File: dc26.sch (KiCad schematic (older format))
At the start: 60 parts, among them J1 CONN_01X10, J2 CONN_01X10, J3 CONN_01X10, Y1 Crystal

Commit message: Further updates
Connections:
- net +5V: now also B_SHIFT_1.16 (VCC), B_SHIFT_2.16 (VCC)
- net GND: now also B_SHIFT_1.8 (GND), B_SHIFT_2.8 (GND)
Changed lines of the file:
@@
 $EndDescr
-$Comp
-L 74LS165 B_SHIFT_1
-U 1 1 5ACD7519
-P -1800 -5700
-F 0 "B_SHIFT_1" H -1650 -5750 50  0000 C CNN
-F 1 "74LS165" H -1650 -5950 50  0000 C CNN
-F 2 "Housings_SSOP:TSSOP-16_4.4x5mm_Pitch0.65mm" H -1800 -5700 50  0001 C CNN
-F 3 "" H -1800 -5700 50  0001 C CNN
-	1    -1800 -5700
-	1    0    0    -1
-$EndComp
 $Comp
 L 74LS165 B_SHIFT_2
@@
 $EndComp
 $Comp
-L GND #PWR18
+L GND #PWR01
 U 1 1 5AD27FBE
-P -3800 -6700
-F 0 "#PWR18" H -3800 -6950 50  0001 C CNN
-F 1 "GND" H -3800 -6850 50  0000 C CNN
-F 2 "" H -3800 -6700 50  0001 C CNN
-F 3 "" H -3800 -6700 50  0001 C CNN
-	1    -3800 -6700
-	-1   0    0    1
-$EndComp
-$Comp
-L GND #PWR2
+P -3450 -6450
+F 0 "#PWR01" H -3450 -6700 50  0001 C CNN
+F 1 "GND" H -3450 -6600 50  0000 C CNN
+F 2 "" H -3450 -6450 50  0001 C CNN
+F 3 "" H -3450 -6450 50  0001 C CNN
+	1    -3450 -6450
+	1    0    0    -1
+$EndComp
+$Comp
+L GND #PWR02
 U 1 1 5AD5BD83
 P -12550 1050
-F 0 "#PWR2" H -12550 800 50  0001 C CNN
+F 0 "#PWR02" H -12550 800 50  0001 C CNN
 F 1 "GND" H -12550 900 50  0000 C CNN
 F 2 "" H -12550 1050 50  0001 C CNN
@@
 $EndComp
 $Comp
-L VCC #PWR6
+L VCC #PWR03
 U 1 1 5AD5C4E4
 P -12300 1050
-F 0 "#PWR6" H -12300 900 50  0001 C CNN
+F 0 "#PWR03" H -12300 900 50  0001 C CNN
 F 1 "VCC" H -12300 1200 50  0000 C CNN
 F 2 "" H -12300 1050 50  0001 C CNN
@@
 $EndComp
 $Comp
-L GND #PWR20
+L GND #PWR04
 U 1 1 5AD6E593
 P -2500 -5100
-F 0 "#PWR20" H -2500 -5350 50  0001 C CNN
+F 0 "#PWR04" H -2500 -5350 50  0001 C CNN
 F 1 "GND" H -2500 -5250 50  0000 C CNN
 F 2 "" H -2500 -5100 50  0001 C CNN
@@
 $EndComp
 $Comp
-L GND #PWR21
+L GND #PWR05
 U 1 1 5AD6F999
 P -2500 -3550
-F 0 "#PWR21" H -2500 -3800 50  0001 C CNN
+F 0 "#PWR05" H -2500 -3800 50  0001 C CNN
 F 1 "GND" H -2500 -3700 50  0000 C CNN
 F 2 "" H -2500 -3550 50  0001 C CNN
@@
 $EndComp
 $Comp
-L GND #PWR19
+L GND #PWR06
 U 1 1 5AD77A72
 P -3600 -800
-F 0 "#PWR19" H -3600 -1050 50  0001 C CNN
+F 0 "#PWR06" H -3600 -1050 50  0001 C CNN
 F 1 "GND" H -3600 -950 50  0000 C CNN
 F 2 "" H -3600 -800 50  0001 C CNN
@@
 $EndComp
 $Comp
-L VCC #PWR11
+L VCC #PWR07
 U 1 1 5AD946E2
 P -7100 12550
-F 0 "#PWR11" H -7100 12400 50  0001 C CNN
+F 0 "#PWR07" H -7100 12400 50  0001 C CNN
 F 1 "VCC" H -7100 12700 50  0000 C CNN
 F 2 "" H -7100 12550 50  0001 C CNN
@@
 $EndComp
 $Comp
-L GND #PWR10
+L GND #PWR08
 U 1 1 5AD98D43
 P -7100 12200
-F 0 "#PWR10" H -7100 11950 50  0001 C CNN
+F 0 "#PWR08" H -7100 11950 50  0001 C CNN
 F 1 "GND" H -7100 12050 50  0000 C CNN
 F 2 "" H -7100 12200 50  0001 C CNN
@@
 $EndComp
 $Comp
-L GND #PWR17
+L GND #PWR09
 U 1 1 5ADAF5CF
 P -3950 10600
-F 0 "#PWR17" H -3950 10350 50  0001 C CNN
+F 0 "#PWR09" H -3950 10350 50  0001 C CNN
 F 1 "GND" H -3950 10450 50  0000 C CNN
 F 2 "" H -3950 10600 50  0001 C CNN
@@
 $EndComp
 $Comp
-L GND #PWR15
+L GND #PWR010
 U 1 1 5ADAFD4C
 P -4000 9500
-F 0 "#PWR15" H -4000 9250 50  0001 C CNN
+F 0 "#PWR010" H -4000 9250 50  0001 C CNN
 F 1 "GND" H -4000 9350 50  0000 C CNN
 F 2 "" H -4000 9500 50  0001 C CNN
@@
 $EndComp
 $Comp
-L GND #PWR16
+L GND #PWR011
 U 1 1 5ADB04C2
 P -4000 12400
-F 0 "#PWR16" H -4000 12150 50  0001 C CNN
+F 0 "#PWR011" H -4000 12150 50  0001 C CNN
 F 1 "GND" H -4000 12250 50  0000 C CNN
 F 2 "" H -4000 12400 50  0001 C CNN
@@
 $EndComp
 $Comp
-L GND #PWR12
+L GND #PWR012
 U 1 1 5B04F2A2
 P -7000 8800
-F 0 "#PWR12" H -7000 8550 50  0001 C CNN
+F 0 "#PWR012" H -7000 8550 50  0001 C CNN
 F 1 "GND" H -7000 8650 50  0000 C CNN
 F 2 "" H -7000 8800 50  0001 C CNN
@@
 $EndComp
 $Comp
-L GND #PWR1
+L GND #PWR013
 U 1 1 5B0E23AB
 P -13400 6550
-F 0 "#PWR1" H -13400 6300 50  0001 C CNN
+F 0 "#PWR013" H -13400 6300 50  0001 C CNN
 F 1 "GND" H -13400 6400 50  0000 C CNN
 F 2 "" H -13400 6550 50  0001 C CNN
@@
 $EndComp
 $Comp
-L +3.3V #PWR9
+L +3.3V #PWR014
 U 1 1 5B0D3E01
 P -7200 2050
-F 0 "#PWR9" H -7200 1900 50  0001 C CNN
+F 0 "#PWR014" H -7200 1900 50  0001 C CNN
 F 1 "+3.3V" H -7200 2190 50  0000 C CNN
 F 2 "" H -7200 2050 50  0001 C CNN
@@
 $EndComp
 $Comp
-L GND #PWR7
+L GND #PWR015
 U 1 1 5B0F137D
 P -12250 5250
-F 0 "#PWR7" H -12250 5000 50  0001 C CNN
+F 0 "#PWR015" H -12250 5000 50  0001 C CNN
 F 1 "GND" H -12250 5100 50  0000 C CNN
 F 2 "" H -12250 5250 50  0001 C CNN
@@
 $EndComp
 $Comp
-L GND #PWR13
+L GND #PWR016
 U 1 1 5B0F6A9C
 P -6200 3750
-F 0 "#PWR13" H -6200 3500 50  0001 C CNN
+F 0 "#PWR016" H -6200 3500 50  0001 C CNN
 F 1 "GND" H -6200 3600 50  0000 C CNN
 F 2 "" H -6200 3750 50  0001 C CNN
@@
 $EndComp
 $Comp
-L +3.3V #PWR8
+L +3.3V #PWR017
 U 1 1 5B11C638
 P -11750 3950
-F 0 "#PWR8" H -11750 3800 50  0001 C CNN
+F 0 "#PWR017" H -11750 3800 50  0001 C CNN
 F 1 "+3.3V" H -11750 4090 50  0000 C CNN
 F 2 "" H -11750 3950 50  0001 C CNN
@@
 $EndComp
 $Comp
-L GND #PWR5
+L GND #PWR018
 U 1 1 5B12677B
 P -12400 4350
-F 0 "#PWR5" H -12400 4100 50  0001 C CNN
+F 0 "#PWR018" H -12400 4100 50  0001 C CNN
 F 1 "GND" H -12400 4200 50  0000 C CNN
 F 2 "" H -12400 4350 50  0001 C CNN
@@
 $EndComp
 $Comp
-L GND #PWR4
+L GND #PWR019
 U 1 1 5B1309D3
 P -12450 4950
-F 0 "#PWR4" H -12450 4700 50  0001 C CNN
+F 0 "#PWR019" H -12450 4700 50  0001 C CNN
 F 1 "GND" H -12450 4800 50  0000 C CNN
 F 2 "" H -12450 4950 50  0001 C CNN
@@
 $EndComp
 $Comp
-L +3.3V #PWR3
+L +3.3V #PWR020
 U 1 1 5B136E3C
 P -12450 4750
-F 0 "#PWR3" H -12450 4600 50  0001 C CNN
+F 0 "#PWR020" H -12450 4600 50  0001 C CNN
 F 1 "+3.3V" H -12450 4890 50  0000 C CNN
 F 2 "" H -12450 4750 50  0001 C CNN
@@
 $EndComp
 $Comp
-L GND #PWR22
+L GND #PWR021
 U 1 1 5B13B631
 P -1800 6650
-F 0 "#PWR22" H -1800 6400 50  0001 C CNN
+F 0 "#PWR021" H -1800 6400 50  0001 C CNN
 F 1 "GND" H -1800 6500 50  0000 C CNN
 F 2 "" H -1800 6650 50  0001 C CNN
@@
 $EndComp
 $Comp
-L GND #PWR23
+L GND #PWR022
 U 1 1 5B1B7467
 P -1200 9050
-F 0 "#PWR23" H -1200 8800 50  0001 C CNN
+F 0 "#PWR022" H -1200 8800 50  0001 C CNN
 F 1 "GND" H -1200 8900 50  0000 C CNN
 F 2 "" H -1200 9050 50  0001 C CNN
@@
 Connection ~ -4300 -3750
 Wire Wire Line
-	-3800 -6700 -3800 -6550
-Wire Wire Line
-	-4000 -6550 -3450 -6550
-Wire Wire Line
 	-4000 -6550 -4000 -3900
 Connection ~ -4000 -6250
@@
 Connection ~ -13250 6150
 $Comp
-L +5V #PWR14
+L +5V #PWR023
 U 1 1 5B123F56
 P -5650 -6600
-F 0 "#PWR14" H -5650 -6750 50  0001 C CNN
+F 0 "#PWR023" H -5650 -6750 50  0001 C CNN
 F 1 "+5V" H -5650 -6460 50  0000 C CNN
 F 2 "" H -5650 -6600 50  0001 C CNN
@@
 Wire Wire Line
 	-2700 6250 -1550 6250
-$Comp
-L PWR_FLAG #FLG?
-U 1 1 5B18689B
-P -6050 -6500
-F 0 "#FLG?" H -6050 -6425 50  0001 C CNN
-F 1 "PWR_FLAG" H -6050 -6350 50  0000 C CNN
-F 2 "" H -6050 -6500 50  0001 C CNN
-F 3 "" H -6050 -6500 50  0001 C CNN
-	1    -6050 -6500
-	1    0    0    -1
-$EndComp
-Wire Wire Line
-	-6050 -6450 -5650 -6450
-Connection ~ -5650 -6450
-Wire Wire Line
-	-6050 -6450 -6050 -6500
-$Comp
-L PWR_FLAG #FLG?
-U 1 1 5B18707E
-P -3450 -6550
-F 0 "#FLG?" H -3450 -6475 50  0001 C CNN
-F 1 "PWR_FLAG" H -3450 -6400 50  0000 C CNN
-F 2 "" H -3450 -6550 50  0001 C CNN
-F 3 "" H -3450 -6550 50  0001 C CNN
-	1    -3450 -6550
-	1    0    0    -1
-$EndComp
-Connection ~ -3800 -6550
+Wire Wire Line
+	-4000 -6550 -3450 -6550
+Wire Wire Line
+	-3450 -6550 -3450 -6450
+$Comp
+L GND #PWR?
+U 1 1 5B188D2F
+P -1100 -5650
+F 0 "#PWR?" H -1100 -5900 50  0001 C CNN
+F 1 "GND" H -1100 -5800 50  0000 C CNN
+F 2 "" H -1100 -5650 50  0001 C CNN
+F 3 "" H -1100 -5650 50  0001 C CNN
+	1    -1100 -5650
+	1    0    0    -1
+$EndComp
+$Comp
+L 74LS165 B_SHIFT_1
+U 1 1 5ACD7519
+P -1800 -5700
+F 0 "B_SHIFT_1" H -1650 -5750 50  0000 C CNN
+F 1 "74LS165" H -1650 -5950 50  0000 C CNN
+F 2 "Housings_SSOP:TSSOP-16_4.4x5mm_Pitch0.65mm" H -1800 -5700 50  0001 C CNN
+F 3 "" H -1800 -5700 50  0001 C CNN
+	1    -1800 -5700
+	1    0    0    -1
+$EndComp
+Wire Wire Line
+	-1300 -5700 -1100 -5700
+Wire Wire Line
+	-1100 -5700 -1100 -5650
+$Comp
+L +5V #PWR?
+U 1 1 5B1896AE
+P -1100 -5850
+F 0 "#PWR?" H -1100 -6000 50  0001 C CNN
+F 1 "+5V" H -1100 -5710 50  0000 C CNN
+F 2 "" H -1100 -5850 50  0001 C CNN
+F 3 "" H -1100 -5850 50  0001 C CNN
+	1    -1100 -5850
+	1    0    0    -1
+$EndComp
+Wire Wire Line
+	-1300 -5850 -1100 -5850
+$Comp
+L +5V #PWR?
+U 1 1 5B189C3C
+P -1150 -4300
+F 0 "#PWR?" H -1150 -4450 50  0001 C CNN
+F 1 "+5V" H -1150 -4160 50  0000 C CNN
+F 2 "" H -1150 -4300 50  0001 C CNN
+F 3 "" H -1150 -4300 50  0001 C CNN
+	1    -1150 -4300
+	1    0    0    -1
+$EndComp
+$Comp
+L GND #PWR?
+U 1 1 5B189D37
+P -1150 -4150
+F 0 "#PWR?" H -1150 -4400 50  0001 C CNN
+F 1 "GND" H -1150 -4300 50  0000 C CNN
+F 2 "" H -1150 -4150 50  0001 C CNN
+F 3 "" H -1150 -4150 50  0001 C CNN
+	1    -1150 -4150
+	1    0    0    -1
+$EndComp
+Wire Wire Line
+	-1300 -4300 -1150 -4300
+Wire Wire Line
+	-1150 -4150 -1300 -4150
 $EndSCHEMATC

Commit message: Changing tp silkscreen names
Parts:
- removed CON_IR1: CONN_01X07, Connectors_JST:JST_PH_B8B-PH-SM4-TB_08x2.00mm_Straight, symbol CONN_01X07
- removed IR_RX_F1, IR_RX_L2, IR_RX_R2: TSOP38238, custom-footprints:IR_Receiver, symbol TSOP38238
- removed IR_RX_L1, IR_RX_R1, IR_TX_F1: IR204A, LEDs:LED_0603, symbol IR204A
- removed R1, R2, R3: 100R, Resistors_SMD:R_0603, symbol R
- TP-BOOT0: value TP-BOOT0 -> BOOT0
- TP-BTN-CLK1: value TP-BTN-CLK -> BTN-CLK
- TP-BTN-DATA1: value TP-BTN-DATA -> BTN-DATA
- TP-BTN-GND1: value TP-BTN-GND -> BTN-GND
- TP-BTN-LOAD1: value TP-BTN-LOAD -> BTN-LD
- TP-NRST1: value TP-NRST -> NRST
- TP-PGM-GND1: value TP-PGM-GND -> PGM-GND
- TP-PGM-SWDCLK1: value TP-PGM-SWDCLK -> PGM-SWDCLK
- TP-PGM-SWDIO1: value TP-PGM-SWDIO -> PGM-SWDIO
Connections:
- net IR-TX-R: now reaches J3.5 (P5), STM32F405.29 (I2C2_SCL/I2S2_CK/SPI2_SCK/TIM2_CH3/USART3_TX/USB_OTG_HS_ULPI_D3/PB10)
- net IR-RX-R: now reaches J3.6 (P6), STM32F405.30 (ADC1_EXTI11/ADC2_EXTI11/ADC3_EXTI11/I2C2_SDA/TIM2_CH4/USART3_RX/USB_OTG_HS_ULPI_D4/PB11)
- net IR-TX-F: now reaches J2.10 (P10), STM32F405.51 (PC10/I2S3_CK/SDIO_D2/SPI3_SCK/UART4_TX/USART3_TX)
- net IR-RX-F: now reaches J2.9 (P9), STM32F405.52 (PC11/ADC1_EXTI11/ADC2_EXTI11/ADC3_EXTI11/I2S3_ext_SD/SDIO_D3/SPI3_MISO/UART4_RX/USART3_RX)
- net IR-TX-L: now reaches J3.1 (P1), STM32F405.58 (CAN2_TX/I2C1_SCL/TIM4_CH1/USART1_TX/PB6)
- net IR-RX-L: now reaches J3.2 (P2), STM32F405.59 (I2C1_SDA/TIM4_CH2/USART1_RX/PB7)
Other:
- moved on the sheet: J1, J2

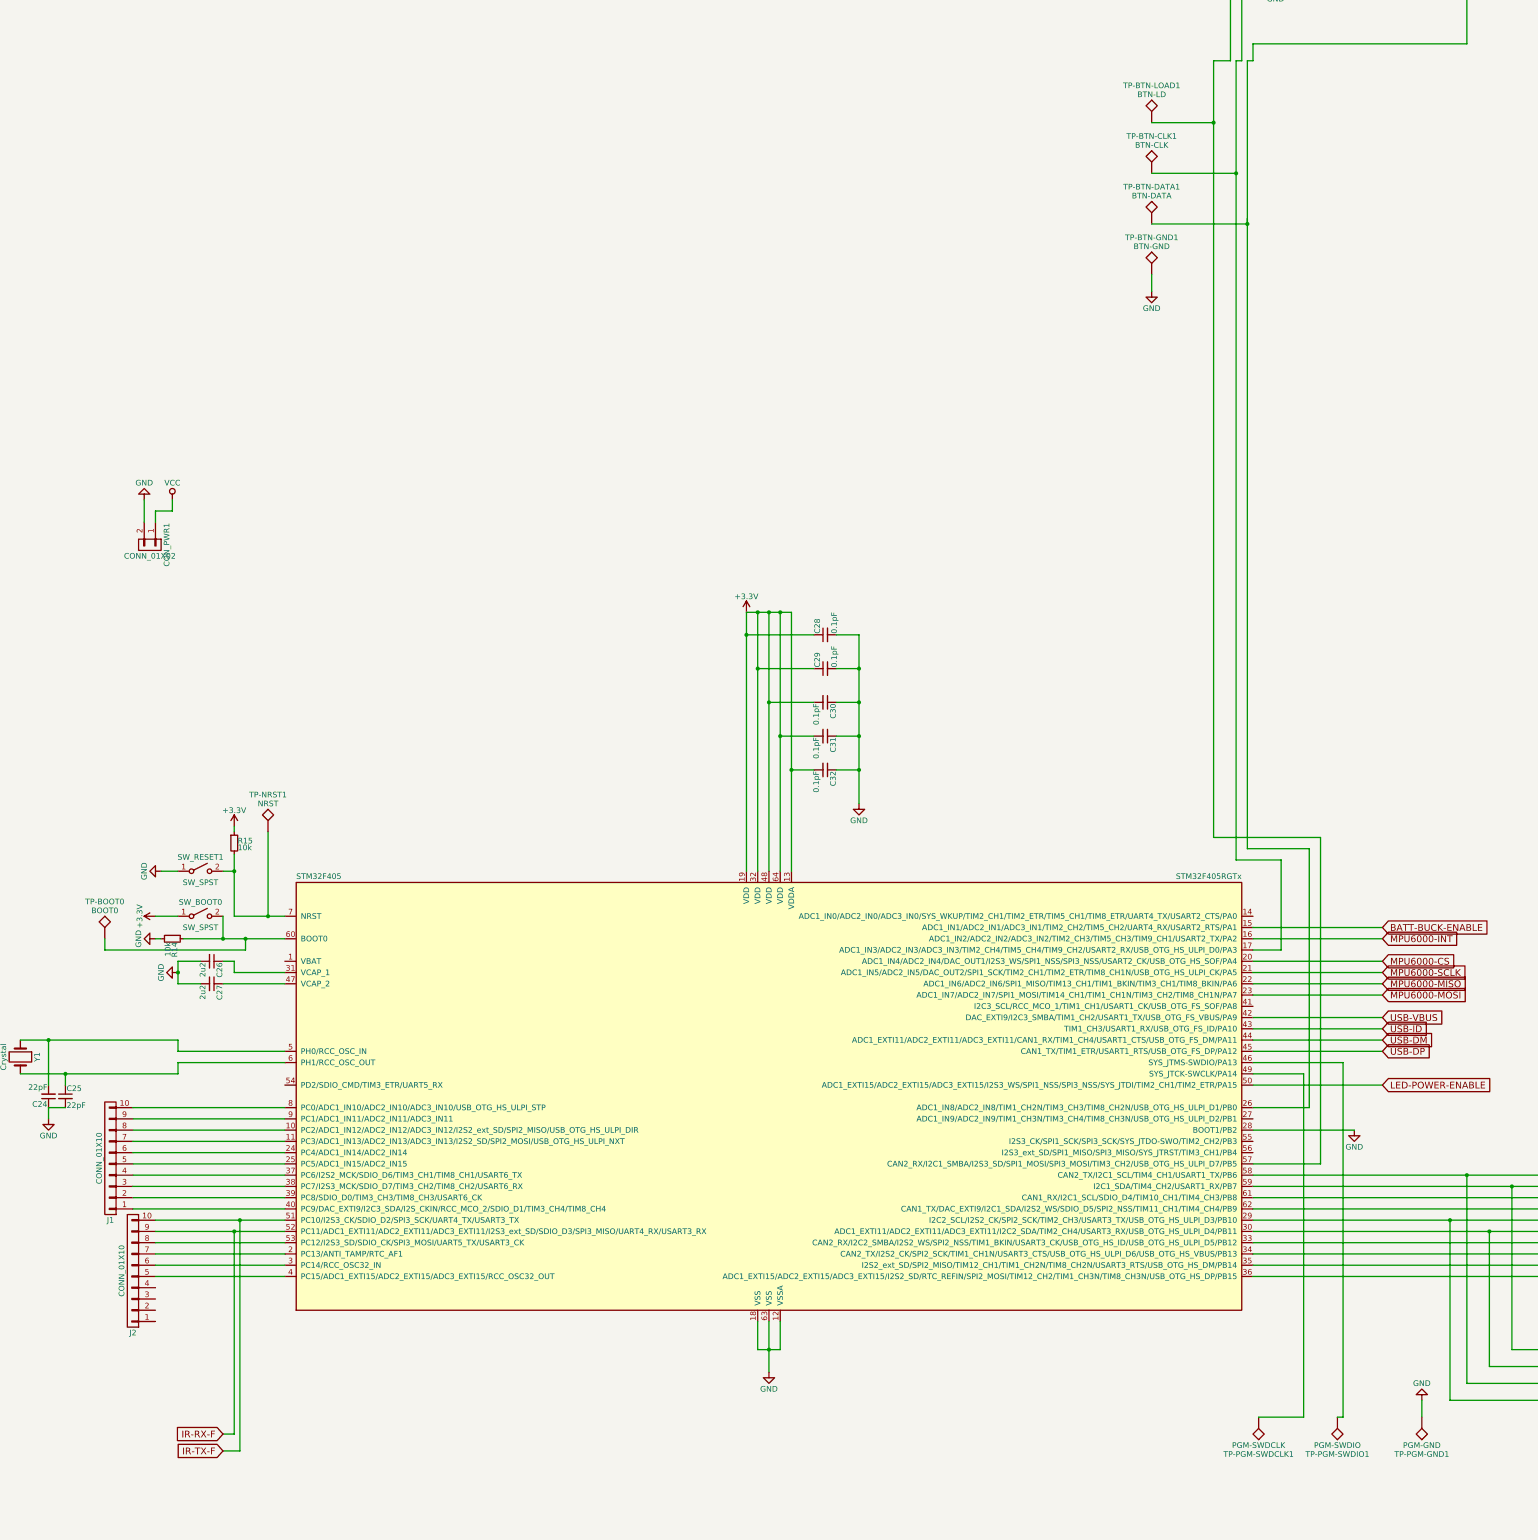
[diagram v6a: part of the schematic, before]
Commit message: tp name fixes
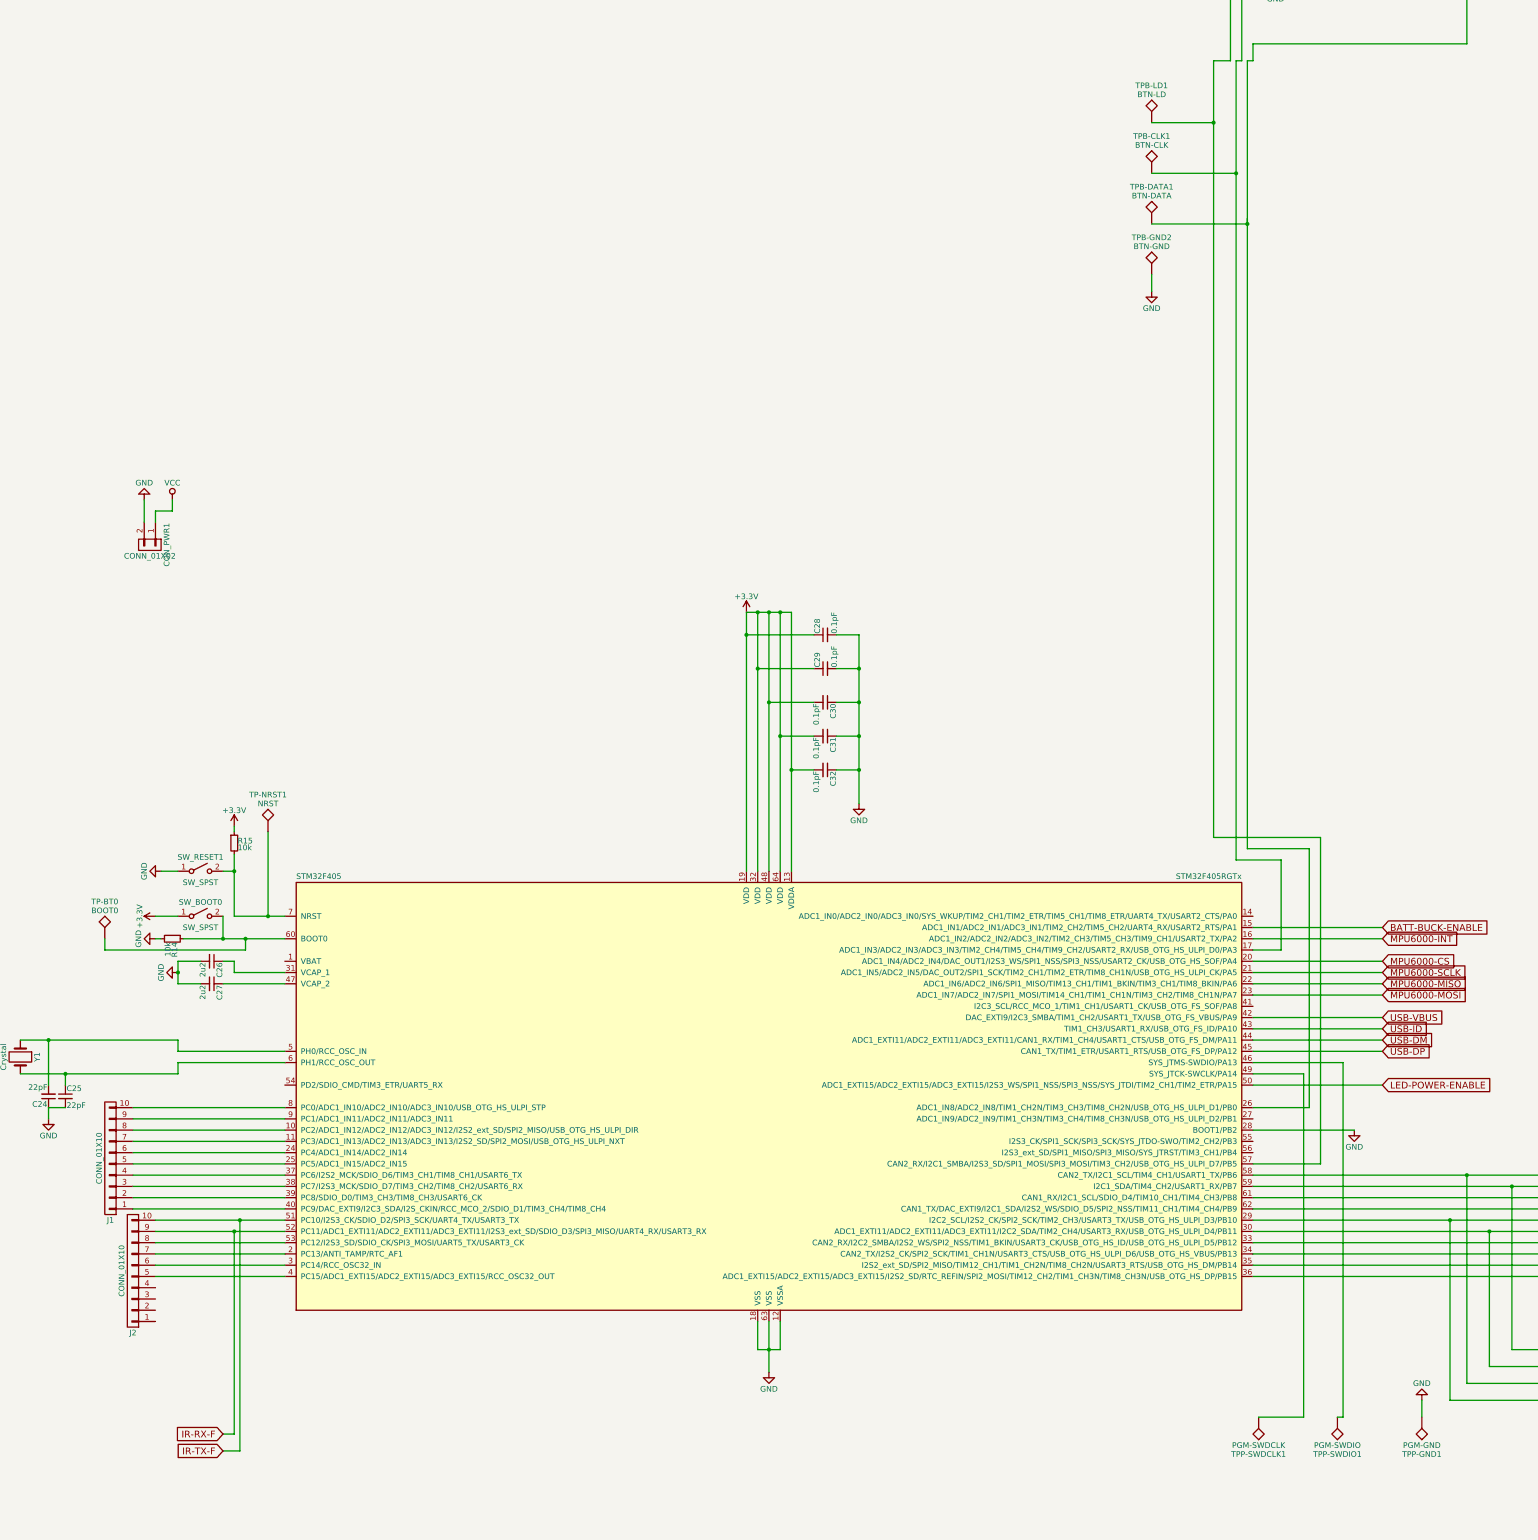
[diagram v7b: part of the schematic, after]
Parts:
- renumbered TP-BOOT0 to TP-BT0, TP-BTN-CLK1 to TPB-CLK1, TP-BTN-DATA1 to TPB-DATA1, TP-BTN-GND1 to TPB-GND2, TP-BTN-LOAD1 to TPB-LD1, TP-PGM-GND1 to TPP-GND1, TP-PGM-SWDCLK1 to TPP-SWDCLK1, TP-PGM-SWDIO1 to TPP-SWDIO1
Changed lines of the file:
@@
 $EndComp
 $Comp
-L TEST TP-PGM-SWDCLK1
+L TEST TPP-SWDCLK1
 U 1 1 5B1B5199
 P -2650 9200
-F 0 "TP-PGM-SWDCLK1" H -2650 9500 50  0000 C BNN
+F 0 "TPP-SWDCLK1" H -2650 9500 50  0000 C BNN
 F 1 "PGM-SWDCLK" H -2650 9450 50  0000 C CNN
 F 2 "Measurement_Points:Measurement_Point_Round-SMD-Pad_Small" H -2650 9200 50  0001 C CNN
@@
 $EndComp
 $Comp
-L TEST TP-PGM-SWDIO1
+L TEST TPP-SWDIO1
 U 1 1 5B1B59E8
 P -1950 9200
-F 0 "TP-PGM-SWDIO1" H -1950 9500 50  0000 C BNN
+F 0 "TPP-SWDIO1" H -1950 9500 50  0000 C BNN
 F 1 "PGM-SWDIO" H -1950 9450 50  0000 C CNN
 F 2 "Measurement_Points:Measurement_Point_Round-SMD-Pad_Small" H -1950 9200 50  0001 C CNN
@@
 $EndComp
 $Comp
-L TEST TP-PGM-GND1
+L TEST TPP-GND1
 U 1 1 5B1B6C72
 P -1200 9200
-F 0 "TP-PGM-GND1" H -1200 9500 50  0000 C BNN
+F 0 "TPP-GND1" H -1200 9500 50  0000 C BNN
 F 1 "PGM-GND" H -1200 9450 50  0000 C CNN
 F 2 "Measurement_Points:Measurement_Point_Round-SMD-Pad_Small" H -1200 9200 50  0001 C CNN
@@
 $EndComp
 $Comp
-L TEST TP-BOOT0
+L TEST TP-BT0
 U 1 1 5B1D1428
 P -12900 4950
-F 0 "TP-BOOT0" H -12900 5250 50  0000 C BNN
+F 0 "TP-BT0" H -12900 5250 50  0000 C BNN
 F 1 "BOOT0" H -12900 5200 50  0000 C CNN
 F 2 "Measurement_Points:Measurement_Point_Round-SMD-Pad_Small" H -12900 4950 50  0001 C CNN
@@
 $EndSheet
 $Comp
-L TEST TP-BTN-LOAD1
+L TEST TPB-LD1
 U 1 1 5B100C70
 P -3600 -2300
-F 0 "TP-BTN-LOAD1" H -3600 -2000 50  0000 C BNN
+F 0 "TPB-LD1" H -3600 -2000 50  0000 C BNN
 F 1 "BTN-LD" H -3600 -2050 50  0000 C CNN
 F 2 "Measurement_Points:Measurement_Point_Round-SMD-Pad_Small" H -3600 -2300 50  0001 C CNN
@@
 $EndComp
 $Comp
-L TEST TP-BTN-CLK1
+L TEST TPB-CLK1
 U 1 1 5B101294
 P -3600 -1850
-F 0 "TP-BTN-CLK1" H -3600 -1550 50  0000 C BNN
+F 0 "TPB-CLK1" H -3600 -1550 50  0000 C BNN
 F 1 "BTN-CLK" H -3600 -1600 50  0000 C CNN
 F 2 "Measurement_Points:Measurement_Point_Round-SMD-Pad_Small" H -3600 -1850 50  0001 C CNN
@@
 $EndComp
 $Comp
-L TEST TP-BTN-DATA1
+L TEST TPB-DATA1
 U 1 1 5B101492
 P -3600 -1400
-F 0 "TP-BTN-DATA1" H -3600 -1100 50  0000 C BNN
+F 0 "TPB-DATA1" H -3600 -1100 50  0000 C BNN
 F 1 "BTN-DATA" H -3600 -1150 50  0000 C CNN
 F 2 "Measurement_Points:Measurement_Point_Round-SMD-Pad_Small" H -3600 -1400 50  0001 C CNN
@@
 Connection ~ -3050 -2300
 $Comp
-L TEST TP-BTN-GND1
+L TEST TPB-GND2
 U 1 1 5B105815
 P -3600 -950
-F 0 "TP-BTN-GND1" H -3600 -650 50  0000 C BNN
+F 0 "TPB-GND2" H -3600 -650 50  0000 C BNN
 F 1 "BTN-GND" H -3600 -700 50  0000 C CNN
 F 2 "Measurement_Points:Measurement_Point_Round-SMD-Pad_Small" H -3600 -950 50  0001 C CNN
